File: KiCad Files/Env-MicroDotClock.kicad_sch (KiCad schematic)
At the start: 48 parts, among them IC1 IS31FL3730-QFLS2-TR, IC2 IS31FL3730-QFLS2-TR, IC3 IS31FL3730-QFLS2-TR, IC4 IS31FL3730-QFLS2-TR, J1 Conn_01x06_Pin, M1 Dip-14 Socket, M2 Dip-14 Socket, M3 Dip-14 Socket, M4 Dip-14 Socket, M5 Dip-14 Socket, M6 Dip-14 Socket, M7 Dip-14 Socket, M8 Dip-14 Socket, Q1 2SC1815, SW1 SKRK, SW2 SKRK, SW3 SKRK, SW4 SKRK, U1 Raspberry Pi Pico, U3 DS3231M

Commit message: added more buttons, re-worked some bits and pieces here and there.
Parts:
- removed SW1, SW2, SW3, SW4: SKRK, Button_Switch_SMD:SW_Push_SPST_NO_Alps_SKRK, symbol Switch:SW_Push
- added SW1, SW2, SW3, SW4, SW5, SW6: SW_SPST, Button_Switch_SMD:SW_Push_SPST_NO_Alps_SKRK, symbol Switch:SW_SPST
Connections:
- net GND: now also SW1.2 (B), SW2.2 (B), SW3.2 (B), SW4.2 (B), SW5.2 (B), SW6.2 (B)
- net GPIO2: now also SW1.1 (A)
- net GPIO3: now also SW2.1 (A)
- net GPIO4: now also SW3.1 (A)
- net GPIO5: now also SW4.1 (A)
- net GPIO6: now also SW5.1 (A)
- net GPIO7: now reaches U1.10 (GPIO7)
- net GPIO7: now also SW6.1 (A)
- net GPIO9: now reaches U1.11 (GPIO8)
- net GPIO8: now reaches U1.12 (GPIO9)
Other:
- moved on the sheet: H1, H2, H3, H4, U1

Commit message: Re-worked board to have optional VCC source, rear usb and a few other adjustments
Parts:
- added J2: GT-USB-7051, Connector_USB:USB_C_Receptacle_G-Switch_GT-USB-7051x, symbol Connector:USB_C_Receptacle_USB2.0
- added JP1: bridge, Jumper:SolderJumper-2_P1.3mm_Bridged_RoundedPad1.0x1.5mm, symbol Jumper:SolderJumper_2_Bridged
- added JP2, JP3: bridge, Jumper:SolderJumper-2_P1.3mm_Open_RoundedPad1.0x1.5mm, symbol Jumper:SolderJumper_2_Bridged
- added R13, R14: 5.1K 0805, Resistor_SMD:R_0805_2012Metric, symbol Device:R_Small
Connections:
- net +3V3: now also JP1.2 (B); no longer C1.1, C2.1, C3.1, C4.1, C5.1, C6.1, C7.1, C8.1, IC1.11 (VCC), IC2.11 (VCC), IC3.11 (VCC), IC4.11 (VCC)
- net GND: now also J2.A1 (GND), J2.A12 (GND), J2.B1 (GND), J2.B12 (GND), J2.S1 (SHIELD), R13.2, R14.2
- net VDD: now reaches U1.39 (VSYS)
- net VDD: now also J2.A4 (VBUS), J2.A9 (VBUS), J2.B4 (VBUS), J2.B9 (VBUS), JP3.2 (B)
- net VBUS: now reaches U1.40 (VBUS)
- net VBUS: now also JP2.2 (B)
- new net: J2.A5 (CC1), R14.1
- new net: J2.B5 (CC2), R13.1
- new net VCC: C1.1, C2.1, C3.1, C4.1, C5.1, C6.1, C7.1, C8.1, IC1.11 (VCC), IC2.11 (VCC), IC3.11 (VCC), IC4.11 (VCC), JP1.1 (A), JP2.1 (A), JP3.1 (A)

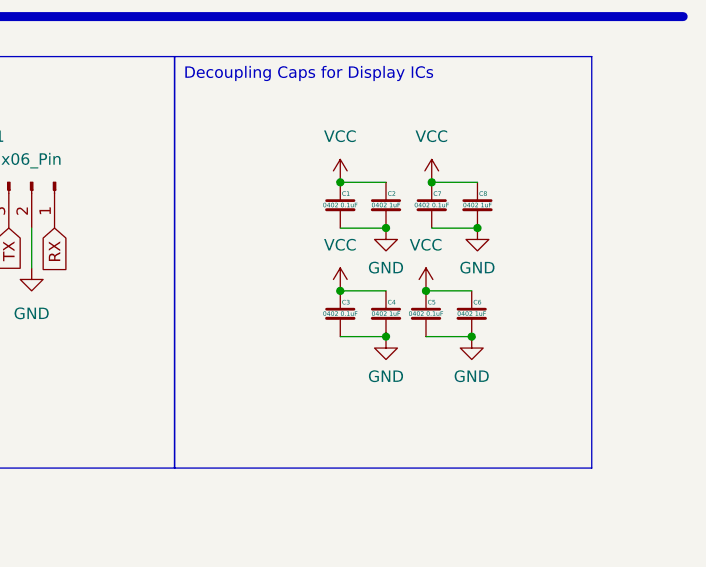
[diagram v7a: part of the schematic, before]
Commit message: removed buzzer so I could fit USB port in a better place, allowing for a pimoroni lipo shim to be installed
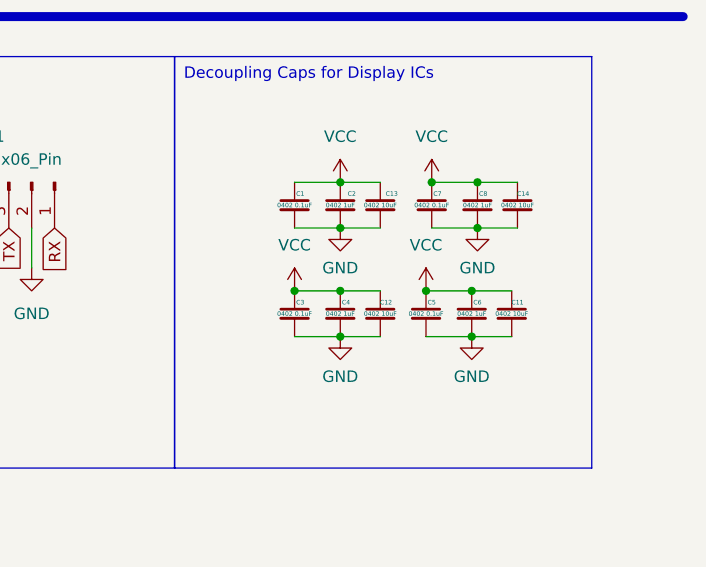
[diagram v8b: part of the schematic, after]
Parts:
- added C11, C12, C13, C14: 0402 10uF, Capacitor_SMD:C_0402_1005Metric, symbol Device:C_Small
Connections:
- net GND: now also C11.2, C12.2, C13.2, C14.2
- net VCC: now also C11.1, C12.1, C13.1, C14.1
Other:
- moved on the sheet: C1, C2, C3, C4
